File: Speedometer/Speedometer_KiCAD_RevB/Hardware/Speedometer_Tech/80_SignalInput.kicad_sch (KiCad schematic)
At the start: 29 parts, among them J800 CTB9302/9, J801 CTB9302/9, U800 CD40109BQNSR, U810 CD40109BQNSR, U820 CD40109BQNSR, U830 CD40109BQNSR, U840 MCP23017-E/SS

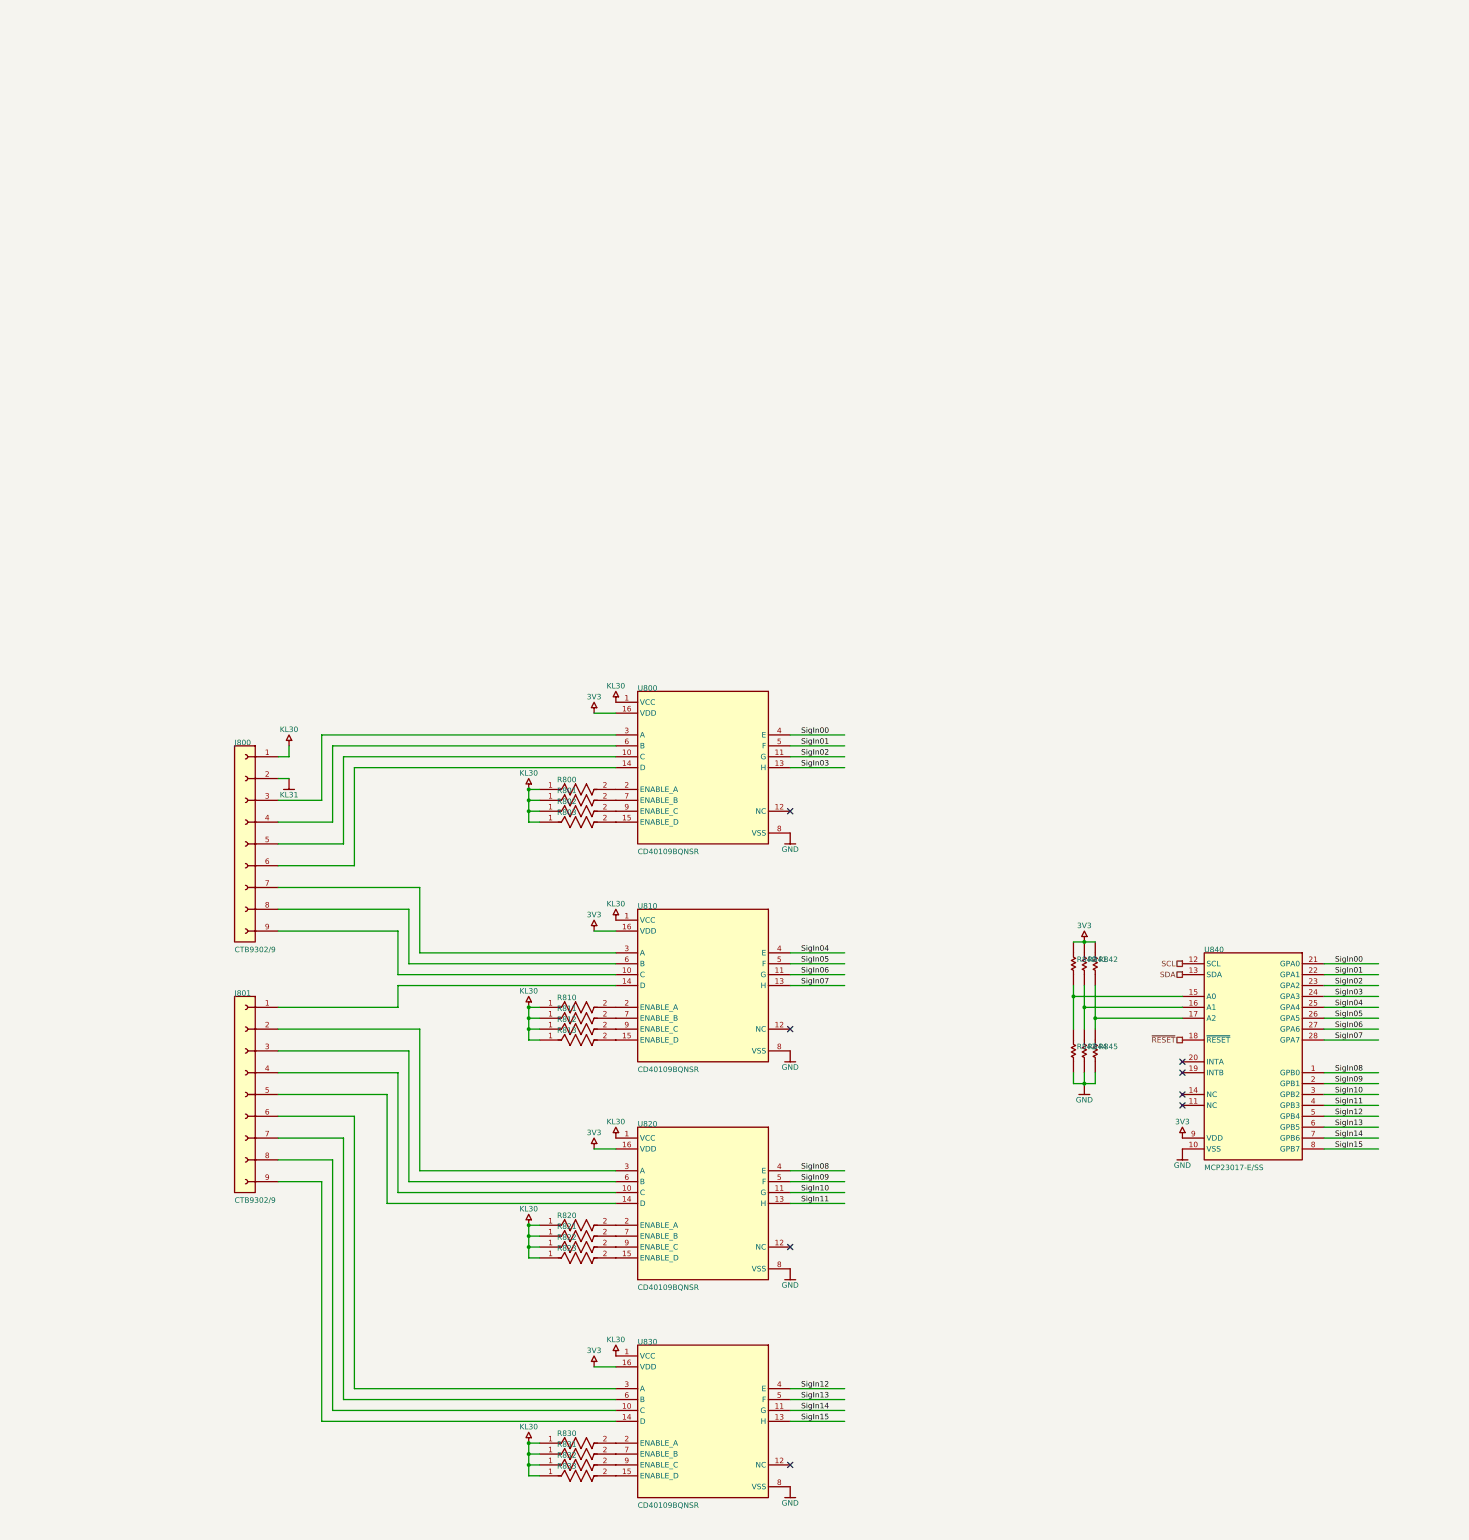
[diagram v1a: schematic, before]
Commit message: current version of lada speedometer in kicad
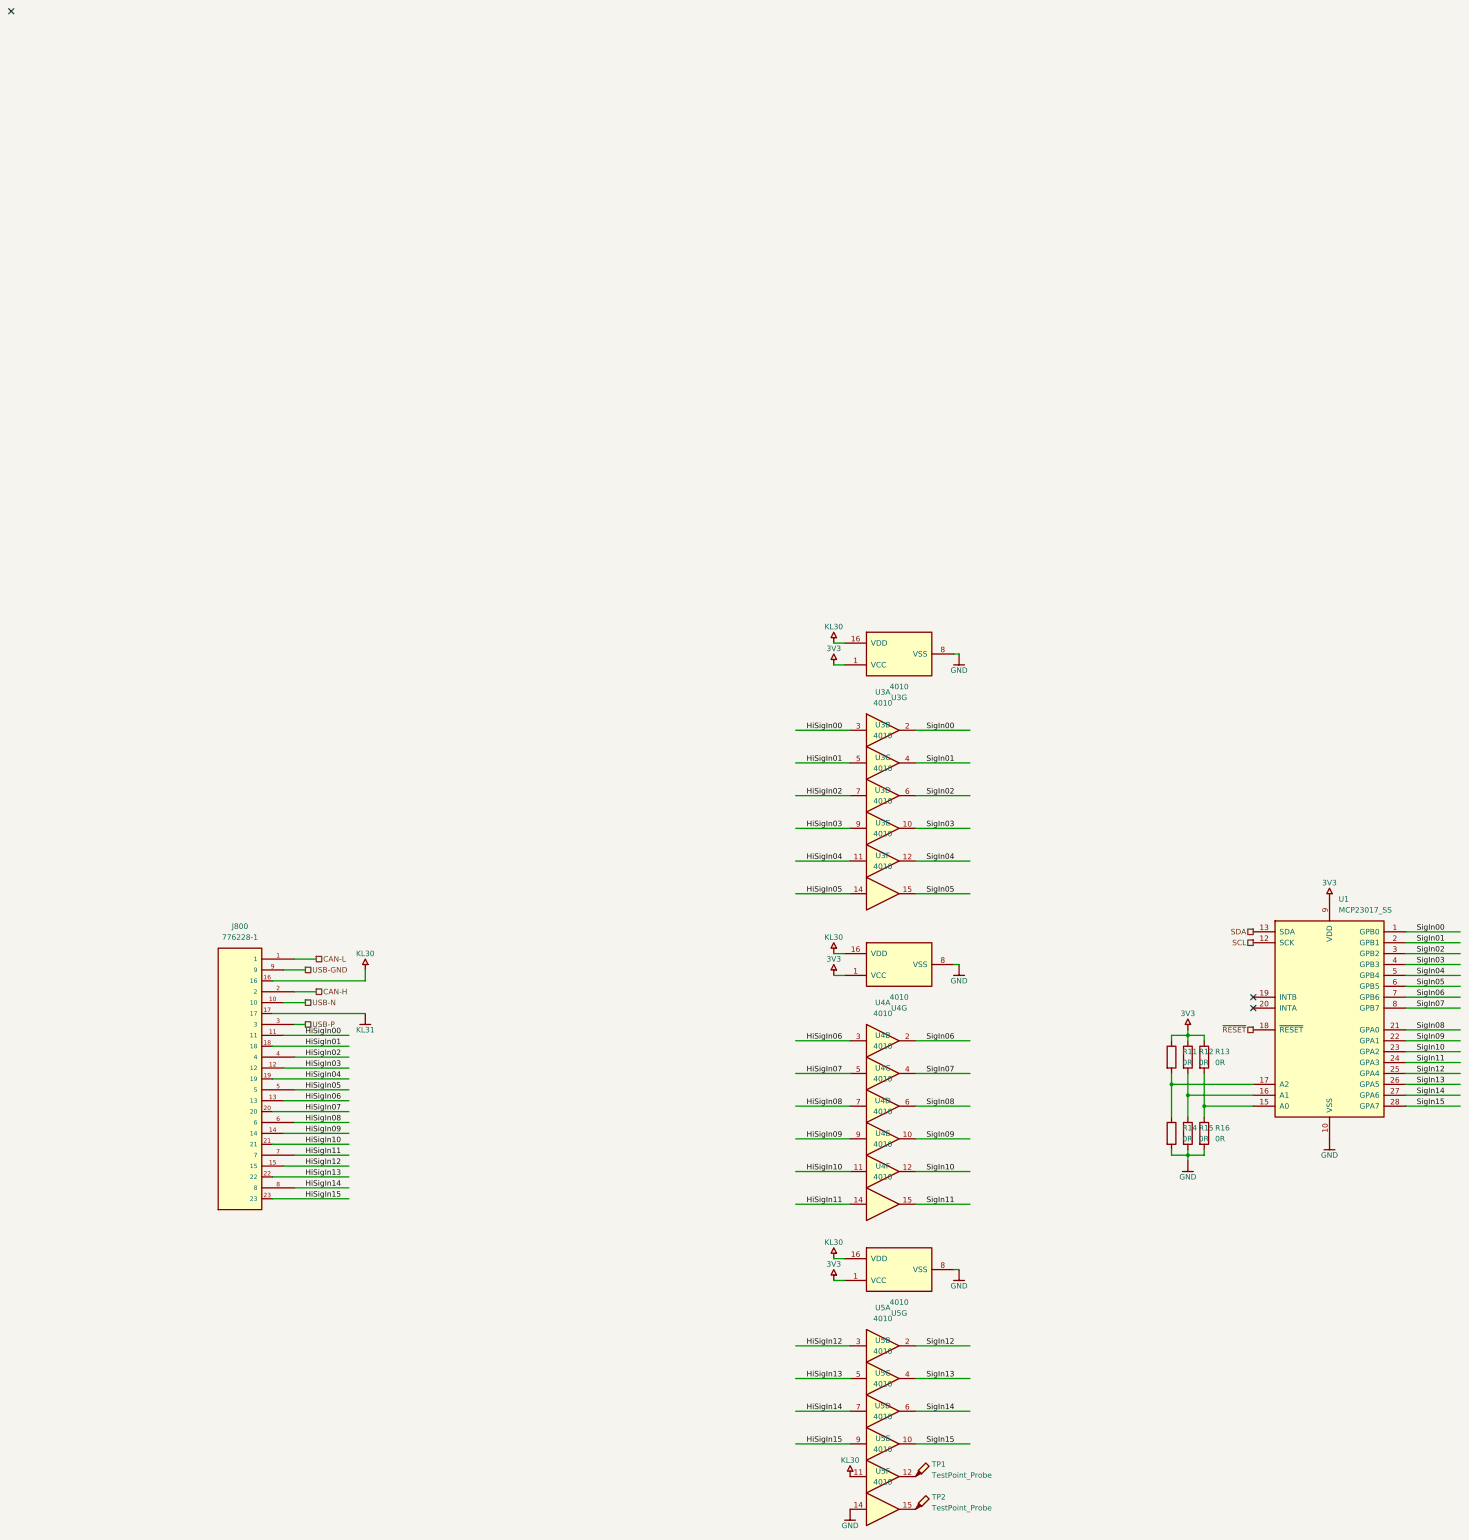
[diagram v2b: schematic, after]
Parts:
- removed J800, J801: CTB9302/9, CTB9302-9, symbol Speedometer_Tech-altium-import:Designator_0_CTB9302-9
- removed R800, R801, R802, R803, R810, R811, R812, R813, R820, R821, R822, R823, R830, R831, R832, R833: AC0603FR-071KL, FP-AC0603-IPC_B, symbol Speedometer_Tech-altium-import:Designator_0_1029c3af85768c4190bb7ad29bc67b5
- removed R840, R841, R842, R843, R844, R845: RC0603JR-070RL, RESC1608X55X25ML10T15, symbol Speedometer_Tech-altium-import:Designator_1_RES-2
- removed U800, U810, U820, U830: CD40109BQNSR, FP-NS0016A-IPC_C, symbol Speedometer_Tech-altium-import:Designator_0_478688682dd803327ab49bead7bebe6
- removed U840: MCP23017-E/SS, SSOP-SS28_N, symbol Speedometer_Tech-altium-import:Designator_0_PR-BUSIC-MCP23017-28
- added J800: 776228-1, Connector_TE-Connectivity:TE_776228-1, symbol Connector:776228-1
- added R11, R12, R13, R14, R15, R16: 0R, symbol Device:R
- added TP1, TP2: TestPoint_Probe, TestPoint:TestPoint_Pad_2.0x2.0mm, symbol Connector:TestPoint_Probe
- added U1: MCP23017_SS, Package_SO:SSOP-28_5.3x10.2mm_P0.65mm, symbol Interface_Expansion:MCP23017_SS
- added U3, U4, U5: 4010, Package_DIP:DIP-16_W7.62mm_LongPads, symbol 4xxx:4010
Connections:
- net 3V3: now also R11.1, R12.1, R13.1, U1.9 (VDD), U3.1 (VCC), U4.1 (VCC), U5.1 (VCC)
- net GND: now also R14.2, R15.2, R16.2, U1.10 (VSS), U3.8 (VSS), U4.8 (VSS), U5.14, U5.8 (VSS)
- net KL30: now also J800.16, U3.16 (VDD), U4.16 (VDD), U5.11, U5.16 (VDD)
- net KL31: now also J800.17
- net SCL: now also U1.12 (SCK)
- net SDA: now also U1.13 (SDA)
- net SigIn00: now also U1.1 (GPB0), U3.2
- net SigIn01: now also U1.2 (GPB1), U3.4
- net SigIn02: now also U1.3 (GPB2), U3.6
- net SigIn03: now also U1.4 (GPB3), U3.10
- net SigIn04: now also U1.5 (GPB4), U3.12
- net SigIn05: now also U1.6 (GPB5), U3.15
- net SigIn06: now also U1.7 (GPB6), U4.2
- net SigIn07: now also U1.8 (GPB7), U4.4
- net SigIn08: now also U1.21 (GPA0), U4.6
- net SigIn09: now also U1.22 (GPA1), U4.10
- net SigIn10: now also U1.23 (GPA2), U4.12
- net SigIn11: now also U1.24 (GPA3), U4.15
- net SigIn12: now also U1.25 (GPA4), U5.2
- net SigIn13: now also U1.26 (GPA5), U5.4
- net SigIn14: now also U1.27 (GPA6), U5.6
- net SigIn15: now also U1.28 (GPA7), U5.10
- net ~{RESET}: now also U1.18 (~{RESET})
- new net: R12.2, R15.1, U1.16 (A1)
- new net: R13.2, R16.1, U1.15 (A0)
- new net: TP2.1, U5.15
- new net: R11.2, R14.1, U1.17 (A2)
- new net: TP1.1, U5.12
- new net CAN-H: J800.2
- new net CAN-L: J800.1
- new net HiSigIn00: J800.11, U3.3
- new net HiSigIn01: J800.18, U3.5
- new net HiSigIn02: J800.4, U3.7
- new net HiSigIn03: J800.12, U3.9
- new net HiSigIn04: J800.19, U3.11
- new net HiSigIn05: J800.5, U3.14
- new net HiSigIn06: J800.13, U4.3
- new net HiSigIn07: J800.20, U4.5
- new net HiSigIn08: J800.6, U4.7
- new net HiSigIn09: J800.14, U4.9
- new net HiSigIn10: J800.21, U4.11
- new net HiSigIn11: J800.7, U4.14
- new net HiSigIn12: J800.15, U5.3
- new net HiSigIn13: J800.22, U5.5
- new net HiSigIn14: J800.8, U5.7
- new net HiSigIn15: J800.23, U5.9
- new net USB-GND: J800.9
- new net USB-N: J800.10
- new net USB-P: J800.3
- no-connect marks 8 -> 3

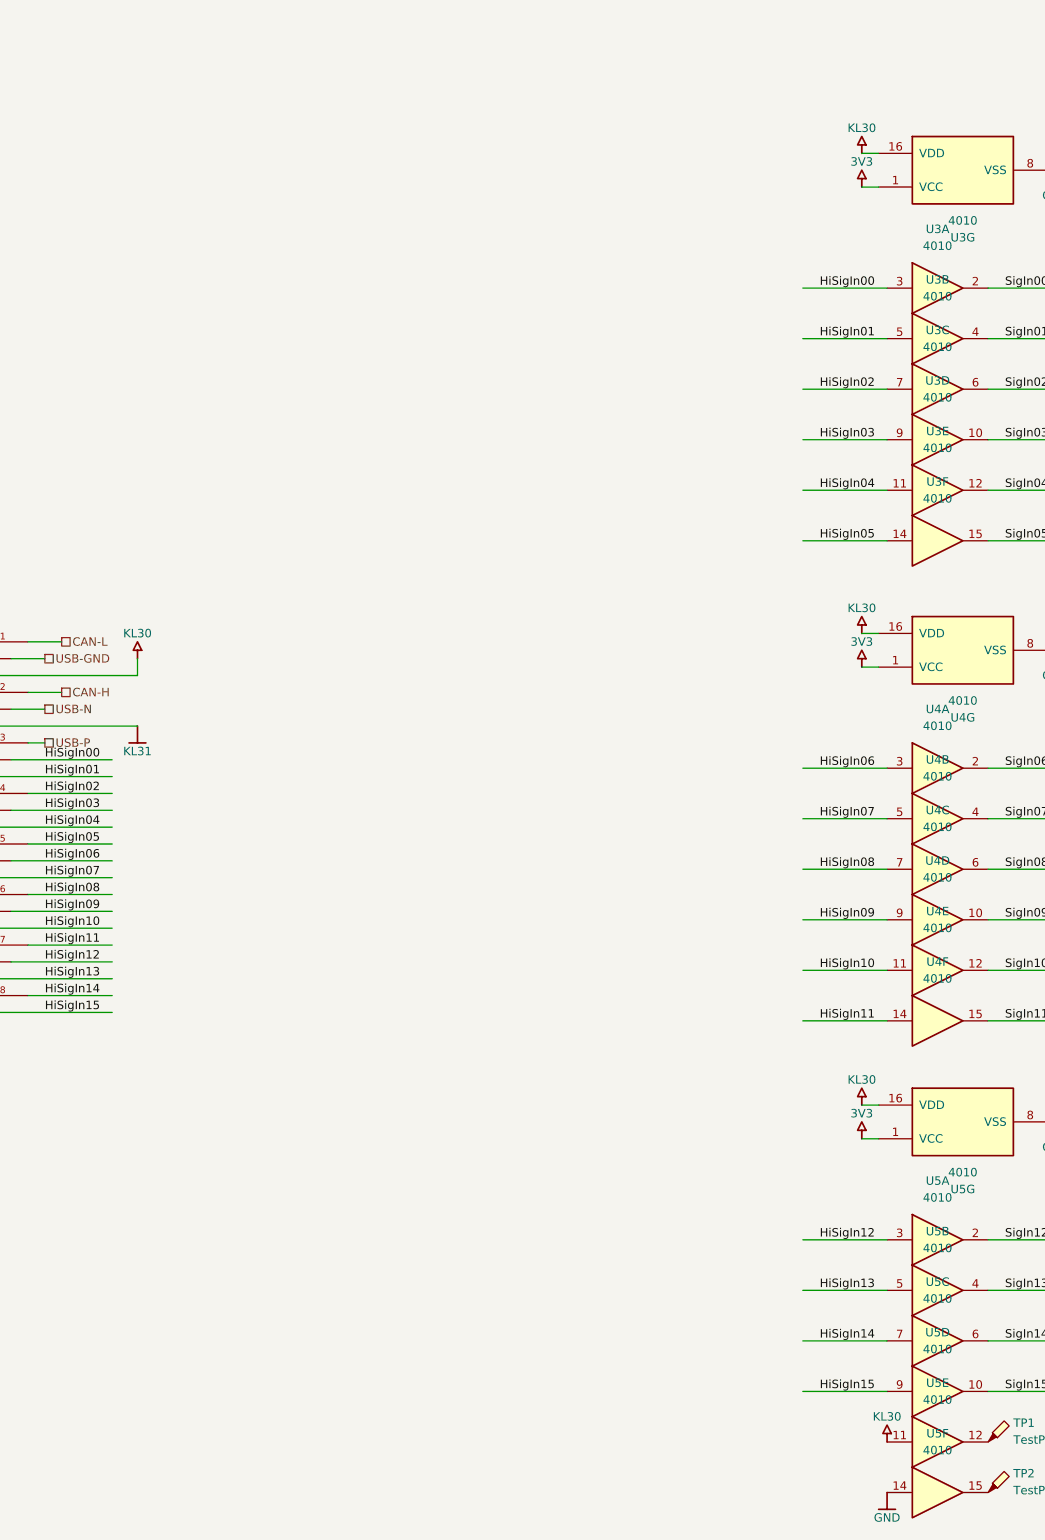
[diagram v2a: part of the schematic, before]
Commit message: Speedometer DRC mostly passed
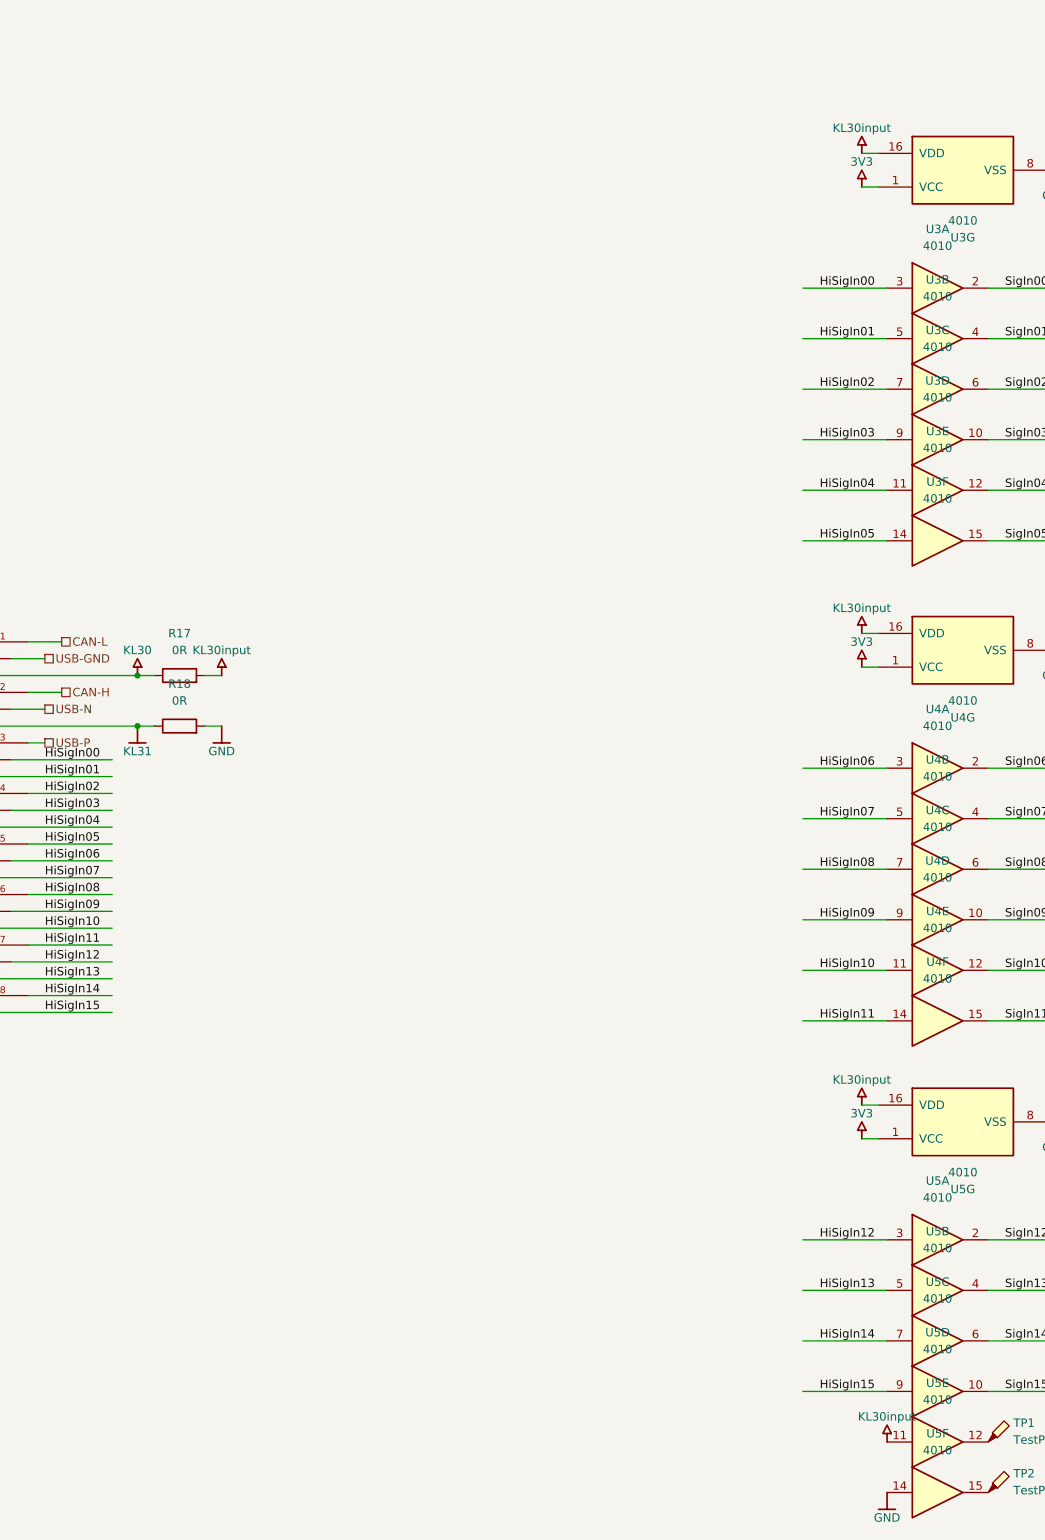
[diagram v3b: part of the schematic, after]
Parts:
- added R17, R18: 0R, Resistor_SMD:R_0603_1608Metric, symbol Device:R
- R11, R12, R13, R14, R15, R16: footprint (none) -> Resistor_SMD:R_0603_1608Metric
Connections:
- net GND: now also R18.2
- net KL30: now also R17.1; no longer U3.16 (VDD), U4.16 (VDD), U5.11, U5.16 (VDD)
- net KL31: now also R18.1
- new net KL30input: R17.2, U3.16 (VDD), U4.16 (VDD), U5.11, U5.16 (VDD)

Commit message: pcb should be done now
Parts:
- R11, R12, R13: now not fitted; now left out of the parts list
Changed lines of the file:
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@@
 		(unit 1)
 		(exclude_from_sim no)
-		(in_bom yes)
+		(in_bom no)
 		(on_board yes)
-		(dnp no)
+		(dnp yes)
 		(fields_autoplaced yes)
 		(property "Reference" "R12"
@@
 		(unit 1)
 		(exclude_from_sim no)
-		(in_bom yes)
+		(in_bom no)
 		(on_board yes)
-		(dnp no)
+		(dnp yes)
 		(fields_autoplaced yes)
 		(property "Reference" "R13"
@@
 		(unit 1)
 		(exclude_from_sim no)
-		(in_bom yes)
+		(in_bom no)
 		(on_board yes)
-		(dnp no)
+		(dnp yes)
 		(fields_autoplaced yes)
 		(property "Reference" "R11"
